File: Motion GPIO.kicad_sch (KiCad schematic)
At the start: 29 parts, among them J401 Fan PWM, J402 GPIO_CONN, Q401 SIL2301-TP, Q402 EM6K7T2R, U401 BNO085, U402 PCA9575HF, Y401 OM-7604-C7

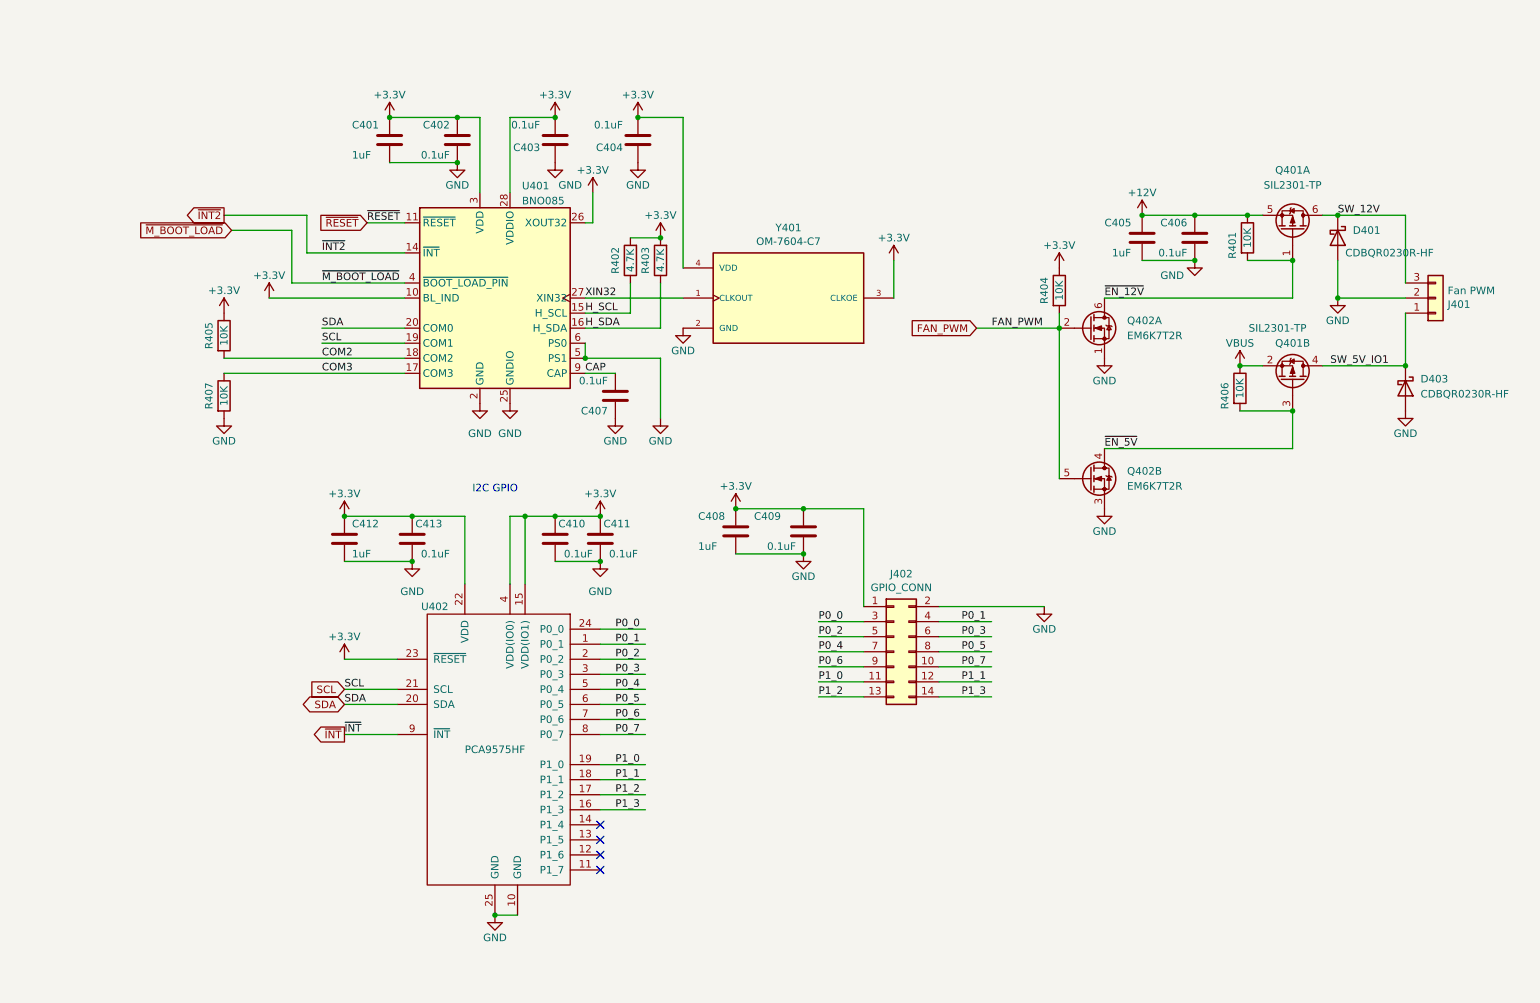
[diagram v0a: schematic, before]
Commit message: More updates
- Changed obsolete unidirectional level shifter to open-collector level shifter
- Replaced BSS138 level shifters with dedicated level shifter
- Changed all 5V I/O pins to have 33 ohm resistor in series
- Changed a few capacitors
- Cleanup tracks, vias, silkscreen, etc.

Signed-off-by: Aaron Williams <aaron.w2@gmail.com>
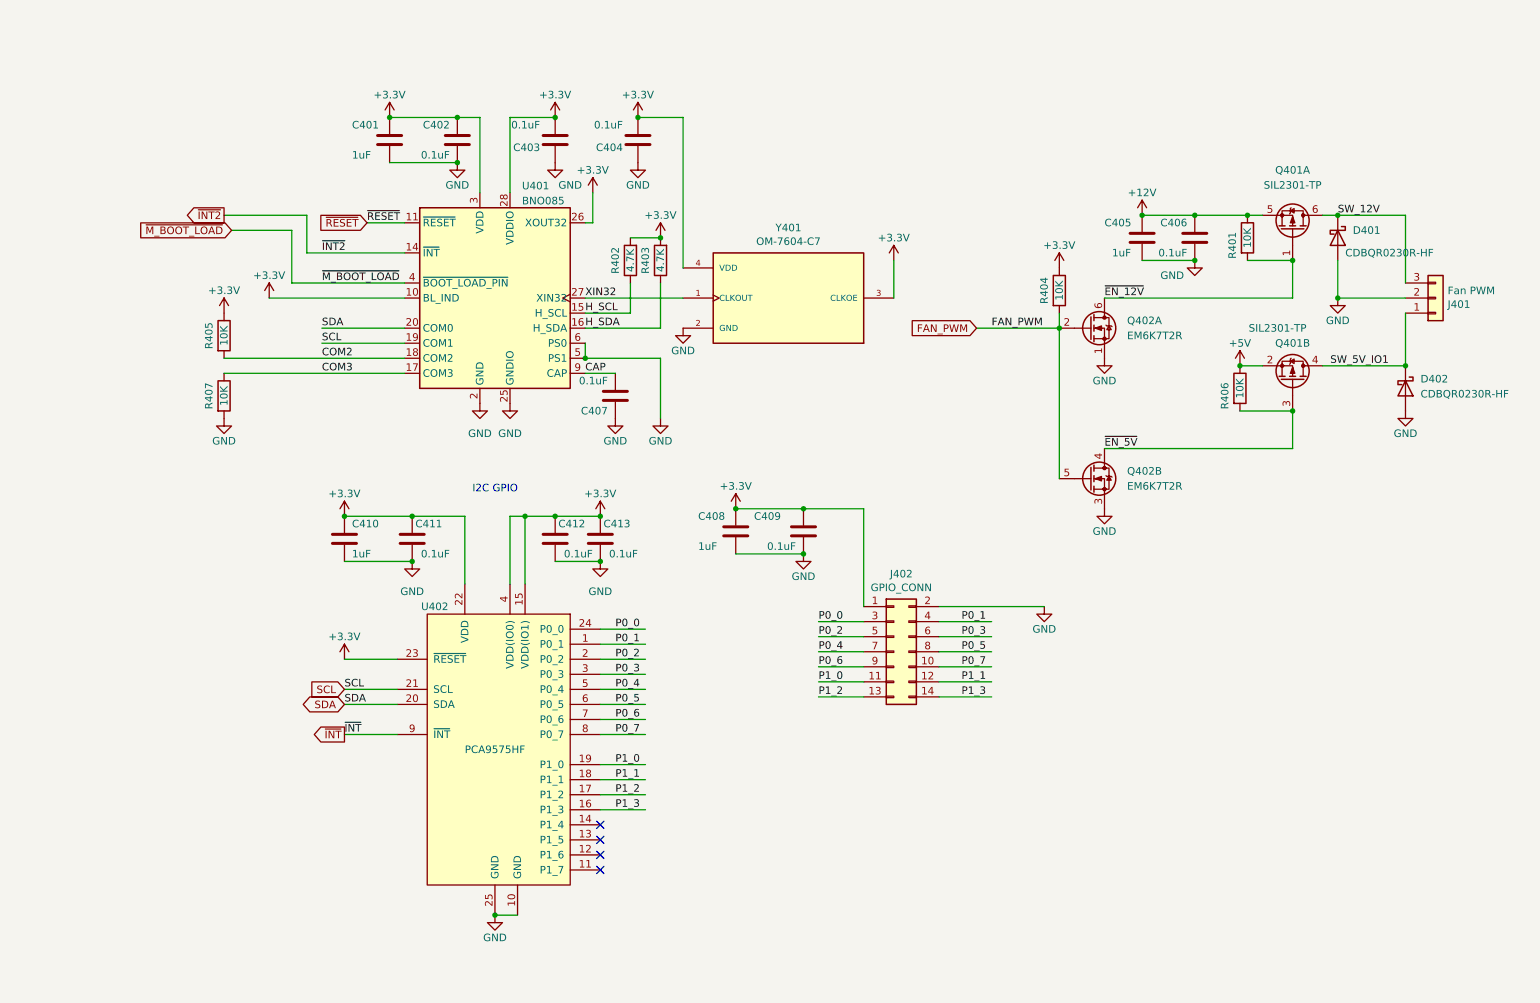
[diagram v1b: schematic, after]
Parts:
- U402: footprint Package_DFN_QFN:HVQFN-24-1EP_4x4mm_P0.5mm_EP2.1x2.1mm -> Aaron:HWQFN-24_EP_4x4_Pitch0.5mm
- renumbered C412 to C410, C413 to C411, C410 to C412, C411 to C413, D403 to D402
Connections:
- net VBUS renamed +5V

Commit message: Multiple updates
- Changed input current limiter to ferrite bead
- Added pull-up for BNO085 boot mode
- Minor layout changes

Signed-off-by: Aaron Williams <aaron.w2@gmail.com>
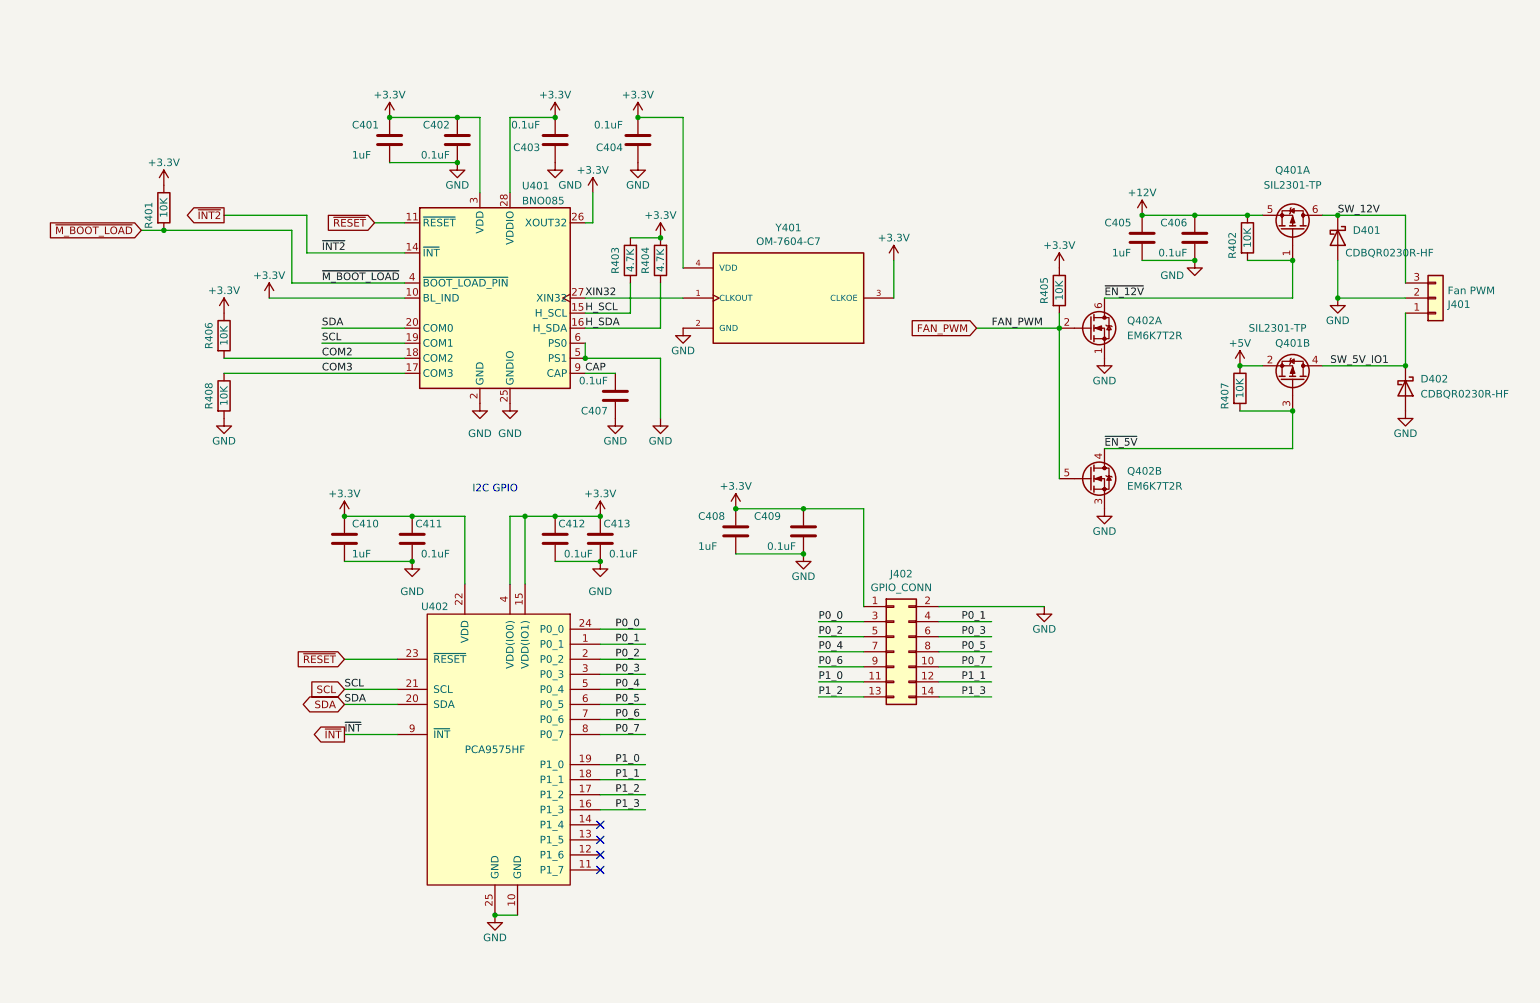
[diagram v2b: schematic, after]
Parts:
- added R401: 10K, Resistor_SMD:R_0402_1005Metric, symbol Device:R
- renumbered R401 to R402, R402 to R403, R403 to R404, R404 to R405, R405 to R406, R406 to R407, R407 to R408
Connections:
- net +3V3: now also R401.1; no longer U402.23 (~{RESET})
- net ~{M_BOOT_LOAD}: now also R401.2
- net ~{RESET}: now also U402.23 (~{RESET})

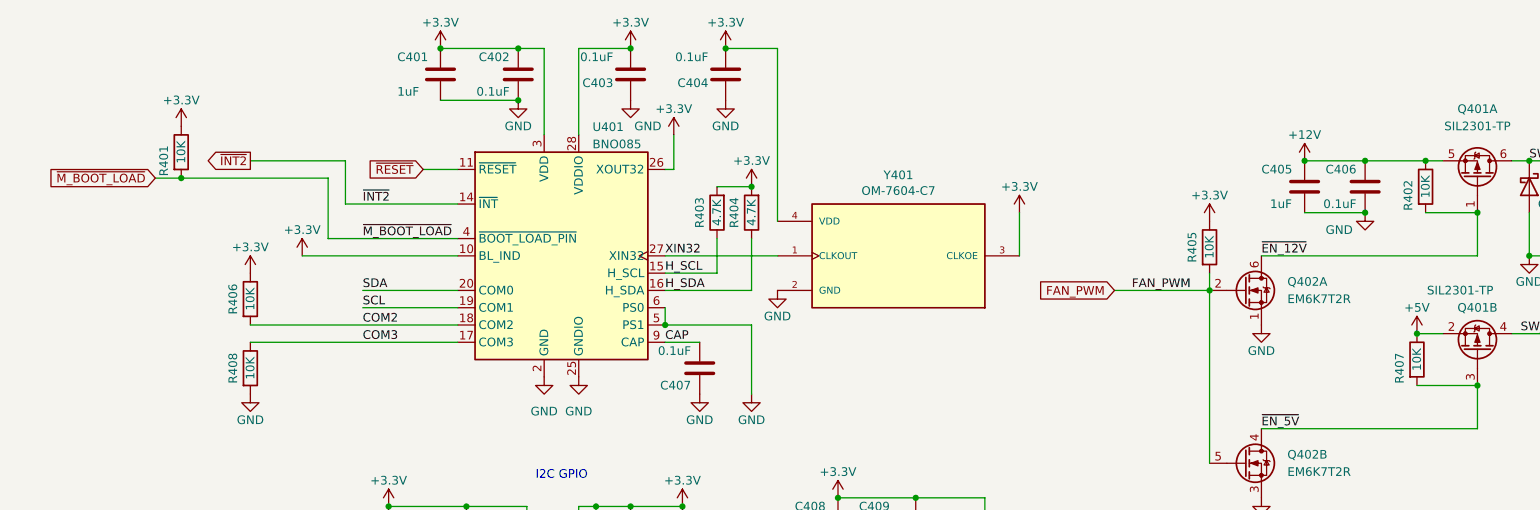
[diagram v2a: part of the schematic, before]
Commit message: More updates
- Removed 5V switch
- Added manual reset control of BNO085 to support booting remotely
- More minor cleanups
- Added jpeg renderings

Signed-off-by: Aaron Williams <aaron.w2@gmail.com>
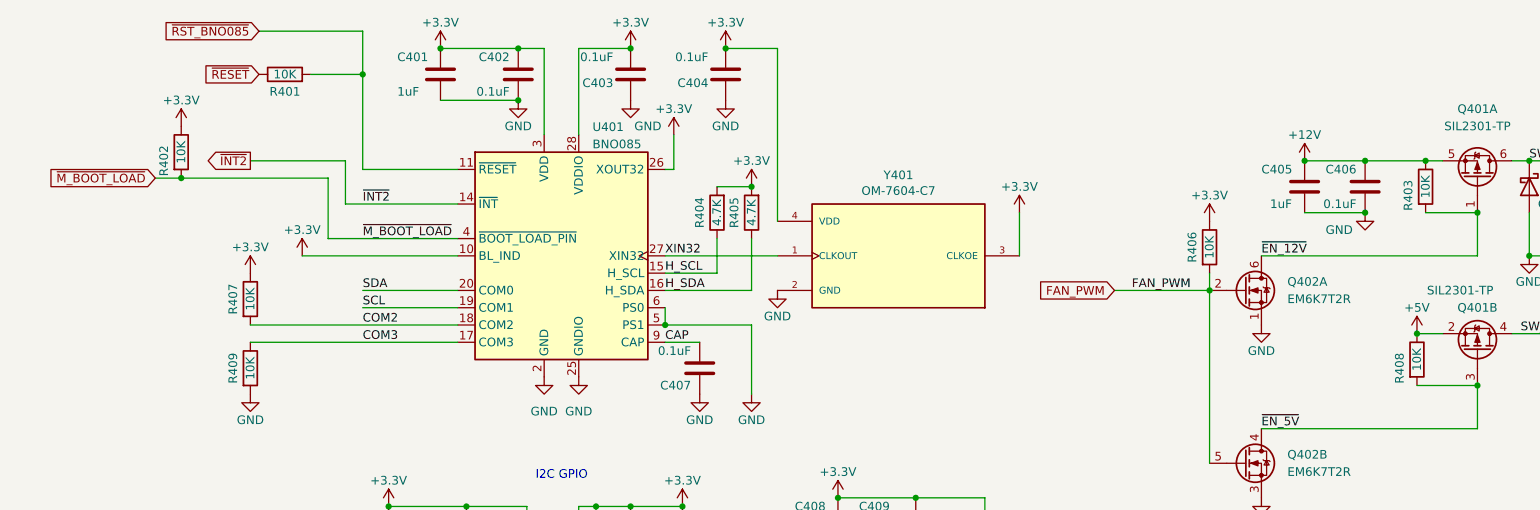
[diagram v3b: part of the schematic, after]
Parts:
- added R401: 10K, Resistor_SMD:R_0402_1005Metric, symbol Device:R
- renumbered R401 to R402, R402 to R403, R403 to R404, R404 to R405, R405 to R406, R406 to R407, R407 to R408, R408 to R409
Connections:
- net ~{RESET}: now also R401.1; no longer U401.11 (~{RESET})
- new net ~{RST_BNO085}: R401.2, U401.11 (~{RESET})
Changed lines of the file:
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@@
   (junction (at 227.33 57.15) (diameter 0) (color 0 0 0 0)
+  )
+  (junction (at 63.5 36.83) (diameter 0) (color 0 0 0 0)
   )
   (junction (at 86.36 33.02) (diameter 0) (color 0 0 0 0)
@@
     (stroke (width 0) (type default) (color 0 0 0 0))
   )
+  (wire (pts (xy 48.26 30.48) (xy 63.5 30.48))
+    (stroke (width 0) (type default) (color 0 0 0 0))
+  )
   (wire (pts (xy 187.96 68.58) (xy 187.96 93.98))
     (stroke (width 0) (type default) (color 0 0 0 0))
@@
     (stroke (width 0) (type default) (color 0 0 0 0))
   )
+  (wire (pts (xy 63.5 36.83) (xy 63.5 50.8))
+    (stroke (width 0) (type default) (color 0 0 0 0))
+  )
   (wire (pts (xy 124.46 33.02) (xy 124.46 58.42))
     (stroke (width 0) (type default) (color 0 0 0 0))
@@
     (stroke (width 0) (type default) (color 0 0 0 0))
   )
+  (wire (pts (xy 63.5 30.48) (xy 63.5 36.83))
+    (stroke (width 0) (type default) (color 0 0 0 0))
+  )
+  (wire (pts (xy 55.88 36.83) (xy 63.5 36.83))
+    (stroke (width 0) (type default) (color 0 0 0 0))
+  )
   (wire (pts (xy 116.84 33.02) (xy 124.46 33.02))
     (stroke (width 0) (type default) (color 0 0 0 0))
@@
     (stroke (width 0) (type default) (color 0 0 0 0))
   )
-  (wire (pts (xy 72.39 50.8) (xy 77.47 50.8))
+  (wire (pts (xy 63.5 50.8) (xy 77.47 50.8))
     (stroke (width 0) (type default) (color 0 0 0 0))
   )
@@
     )
   )
-  (global_label "~{RESET}" (shape input) (at 72.39 50.8 180) (fields_autoplaced)
+  (global_label "~{RESET}" (shape input) (at 48.26 36.83 180) (fields_autoplaced)
     (effects (font (size 1.27 1.27)) (justify right))
-    (property "Intersheet References" "${INTERSHEET_REFS}" (id 0) (at 64.3206 50.7206 0)
+    (property "Intersheet References" "${INTERSHEET_REFS}" (id 0) (at 40.1906 36.7506 0)
       (effects (font (size 1.27 1.27)) (justify right) hide)
     )
@@
     (effects (font (size 1.27 1.27)) (justify right))
     (property "Intersheet References" "${INTERSHEET_REFS}" (id 0) (at 17.6934 51.9906 0)
+      (effects (font (size 1.27 1.27)) (justify right) hide)
+    )
+  )
+  (global_label "~{RST_BNO085}" (shape input) (at 48.26 30.48 180) (fields_autoplaced)
+    (effects (font (size 1.27 1.27)) (justify right))
+    (property "Intersheet References" "${INTERSHEET_REFS}" (id 0) (at 33.9615 30.4006 0)
       (effects (font (size 1.27 1.27)) (justify right) hide)
     )
@@
   (symbol (lib_id "Device:R") (at 46.99 69.85 0) (unit 1)
     (in_bom yes) (on_board yes)
-    (property "Reference" "R406" (id 0) (at 44.45 69.85 90))
+    (property "Reference" "R407" (id 0) (at 44.45 69.85 90))
     (property "Value" "10K" (id 1) (at 46.99 69.85 90))
     (property "Footprint" "Resistor_SMD:R_0402_1005Metric" (id 2) (at 45.212 69.85 90)
@@
   (symbol (lib_id "Device:R") (at 115.57 57.15 180) (unit 1)
     (in_bom yes) (on_board yes)
-    (property "Reference" "R403" (id 0) (at 113.03 57.15 90))
+    (property "Reference" "R404" (id 0) (at 113.03 57.15 90))
     (property "Value" "4.7K" (id 1) (at 115.57 57.15 90))
     (property "Footprint" "Resistor_SMD:R_0402_1005Metric" (id 2) (at 117.348 57.15 90)
@@
   (symbol (lib_id "Device:R") (at 219.71 53.34 0) (unit 1)
     (in_bom yes) (on_board yes)
-    (property "Reference" "R402" (id 0) (at 217.17 54.61 90))
+    (property "Reference" "R403" (id 0) (at 217.17 54.61 90))
     (property "Value" "10K" (id 1) (at 219.71 53.34 90))
     (property "Footprint" "Resistor_SMD:R_0402_1005Metric" (id 2) (at 217.932 53.34 90)
@@
   (symbol (lib_id "Device:R") (at 36.83 48.26 0) (unit 1)
     (in_bom yes) (on_board yes)
-    (property "Reference" "R401" (id 0) (at 34.29 49.53 90))
+    (property "Reference" "R402" (id 0) (at 34.29 49.53 90))
     (property "Value" "10K" (id 1) (at 36.83 48.26 90))
     (property "Footprint" "Resistor_SMD:R_0402_1005Metric" (id 2) (at 35.052 48.26 90)
@@
   (symbol (lib_id "Device:R") (at 187.96 62.23 0) (unit 1)
     (in_bom yes) (on_board yes)
-    (property "Reference" "R405" (id 0) (at 185.42 62.23 90))
+    (property "Reference" "R406" (id 0) (at 185.42 62.23 90))
     (property "Value" "10K" (id 1) (at 187.96 62.23 90))
     (property "Footprint" "Resistor_SMD:R_0402_1005Metric" (id 2) (at 186.182 62.23 90)
@@
   (symbol (lib_id "Device:R") (at 120.65 57.15 180) (unit 1)
     (in_bom yes) (on_board yes)
-    (property "Reference" "R404" (id 0) (at 118.11 57.15 90))
+    (property "Reference" "R405" (id 0) (at 118.11 57.15 90))
     (property "Value" "4.7K" (id 1) (at 120.65 57.15 90))
     (property "Footprint" "Resistor_SMD:R_0402_1005Metric" (id 2) (at 122.428 57.15 90)
@@
   (symbol (lib_id "Device:R") (at 218.44 78.74 0) (unit 1)
     (in_bom yes) (on_board yes)
-    (property "Reference" "R407" (id 0) (at 215.9 80.01 90))
+    (property "Reference" "R408" (id 0) (at 215.9 80.01 90))
     (property "Value" "10K" (id 1) (at 218.44 78.74 90))
     (property "Footprint" "Resistor_SMD:R_0402_1005Metric" (id 2) (at 216.662 78.74 90)
@@
   (symbol (lib_id "Device:R") (at 46.99 80.01 0) (unit 1)
     (in_bom yes) (on_board yes)
-    (property "Reference" "R408" (id 0) (at 44.45 80.01 90))
+    (property "Reference" "R409" (id 0) (at 44.45 80.01 90))
     (property "Value" "10K" (id 1) (at 46.99 80.01 90))
     (property "Footprint" "Resistor_SMD:R_0402_1005Metric" (id 2) (at 45.212 80.01 90)
@@
     (pin "1")
   )
+  (symbol (lib_id "Device:R") (at 52.07 36.83 90) (unit 1)
+    (in_bom yes) (on_board yes)
+    (property "Reference" "R401" (id 0) (at 52.07 39.37 90))
+    (property "Value" "10K" (id 1) (at 52.07 36.83 90))
+    (property "Footprint" "Resistor_SMD:R_0402_1005Metric" (id 2) (at 52.07 38.608 90)
+      (effects (font (size 1.27 1.27)) hide)
+    )
+    (property "Datasheet" "~" (id 3) (at 52.07 36.83 0)
+      (effects (font (size 1.27 1.27)) hide)
+    )
+    (property "Tolerance" "5%" (id 4) (at 52.07 36.83 90)
+      (effects (font (size 1.27 1.27)) hide)
+    )
+    (property "MFR" "" (id 5) (at 95.25 63.5 0)
+      (effects (font (size 1.27 1.27)) hide)
+    )
+    (property "MPN" "" (id 6) (at 95.25 63.5 0)
+      (effects (font (size 1.27 1.27)) hide)
+    )
+    (property "SPR" "Digikey" (id 7) (at 95.25 63.5 0)
+      (effects (font (size 1.27 1.27)) hide)
+    )
+    (property "SPN" "541-2979-1-ND" (id 8) (at 95.25 63.5 0)
+      (effects (font (size 1.27 1.27)) hide)
+    )
+    (property "SPURL" "https://www.digikey.com/products/en?keywords=541-2979-1-ND" (id 9) (at 95.25 63.5 0)
+      (effects (font (size 1.27 1.27)) hide)
+    )
+    (property "DESC" "" (id 10) (at 78.74 62.23 0)
+      (effects (font (size 1.27 1.27)) hide)
+    )
+    (pin "1")
+    (pin "2")
+  )
   (symbol (lib_id "Device:C") (at 116.84 36.83 0) (mirror y) (unit 1)
